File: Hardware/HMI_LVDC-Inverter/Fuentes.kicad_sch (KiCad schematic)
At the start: 33 parts, among them U2 TPS74633PQWDRBRQ1, U4 AP64100SP-13

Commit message: Termino de hacer las simulaciones de los periféricos. Completo los valores de componentes en esquemáticos
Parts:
- C28: footprint Inductor_SMD:L_1206_3216Metric -> Capacitor_SMD:C_1206_3216Metric
- R16: value 680K -> 681K
- R17: value 120K -> 121K
- R18: value 510K -> 511K
- R20: value 39863 -> 40.2K
- R21: value 4759 -> 4K75
- R22: value 500K -> 499K
- R23: value 7.005K -> 6K98
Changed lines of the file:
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@@
 			)
 		)
-		(property "Footprint" "Inductor_SMD:L_1206_3216Metric"
+		(property "Footprint" "Capacitor_SMD:C_1206_3216Metric"
 			(at 153.3652 67.31 0)
 			(effects
@@
 			)
 		)
-		(property "Value" "4759"
+		(property "Value" "4K75"
 			(at 23.114 67.818 0)
 			(effects
@@
 			)
 		)
-		(property "Value" "680K"
+		(property "Value" "681K"
 			(at 215.392 34.29 0)
 			(effects
@@
 			)
 		)
-		(property "Value" "120K"
+		(property "Value" "121K"
 			(at 217.17 44.45 0)
 			(effects
@@
 			)
 		)
-		(property "Value" "7.005K"
+		(property "Value" "6K98"
 			(at 114.554 70.612 0)
 			(effects
@@
 			)
 		)
-		(property "Value" "39863"
+		(property "Value" "40.2K"
 			(at 23.114 57.658 0)
 			(effects
@@
 			)
 		)
-		(property "Value" "510K"
+		(property "Value" "511K"
 			(at 251.206 34.29 0)
 			(effects
@@
 			)
 		)
-		(property "Value" "500K"
+		(property "Value" "499K"
 			(at 92.964 80.518 0)
 			(effects

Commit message: Terminado el esquemático del HMI
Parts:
- removed R14: 1.5M, symbol Device:R_US
- removed R15: 100K, symbol Device:R_US
- C21, C22, C23, C24, C25, C26, C27, C28, C8, L1, L2, R20, R21, R22, R23, R24, R25, U4: now not fitted
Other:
- moved on the sheet: R16, R17, R18, R19

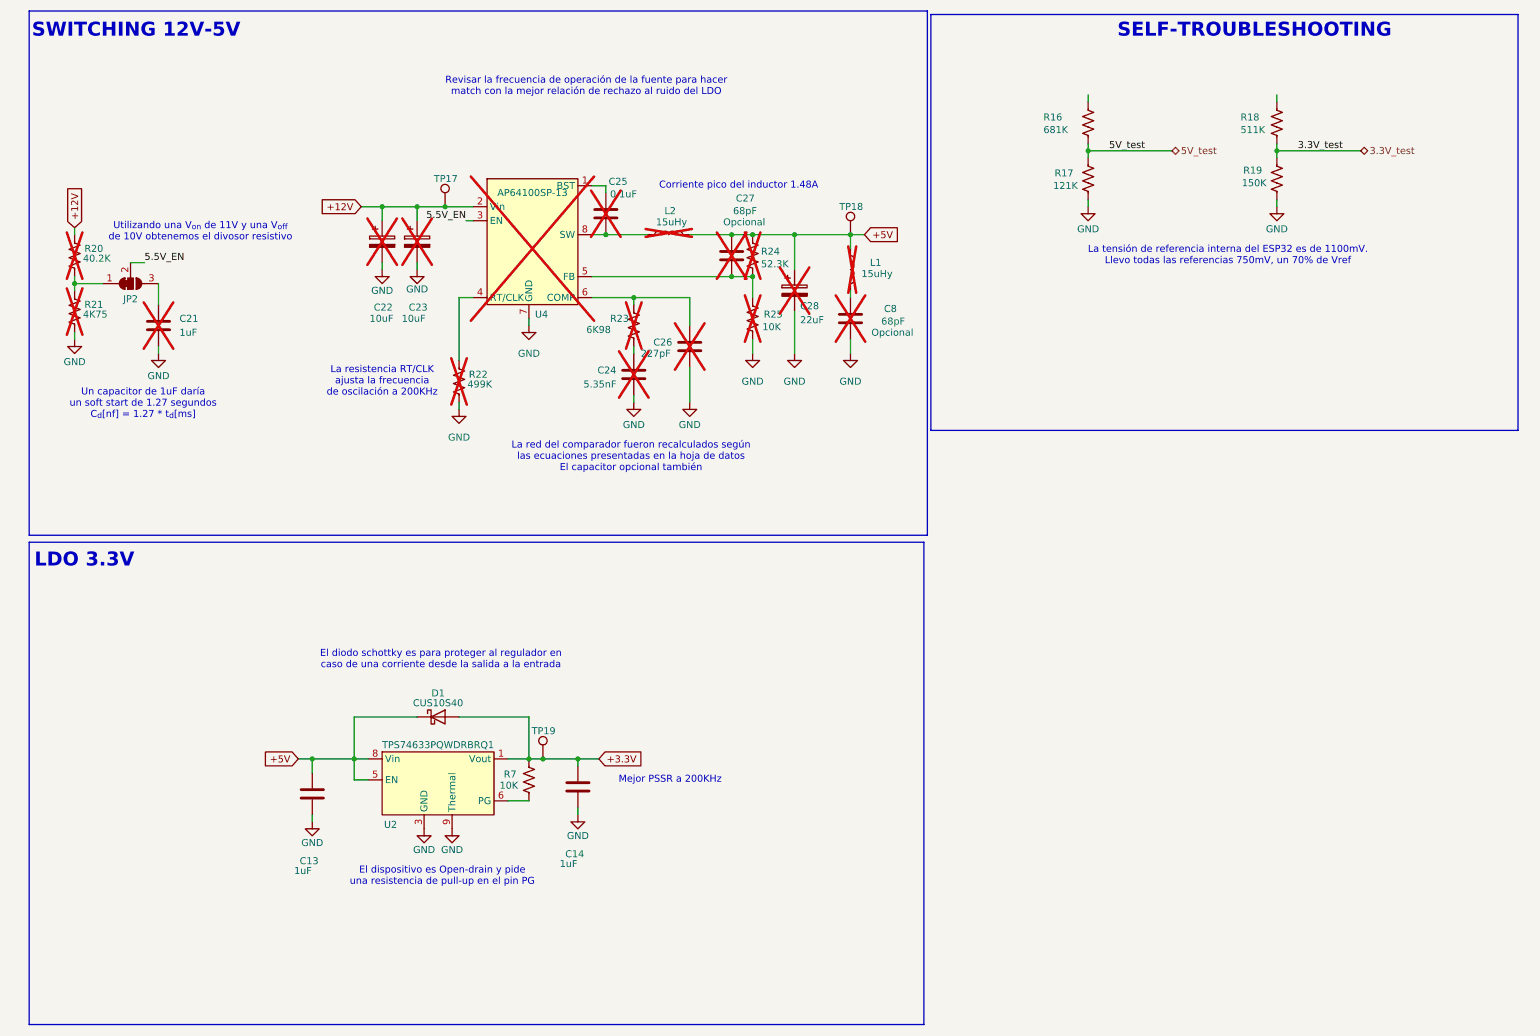
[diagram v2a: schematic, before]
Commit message: Avance con el esquemático, faltan definir algunas etiquetas que no las encontré
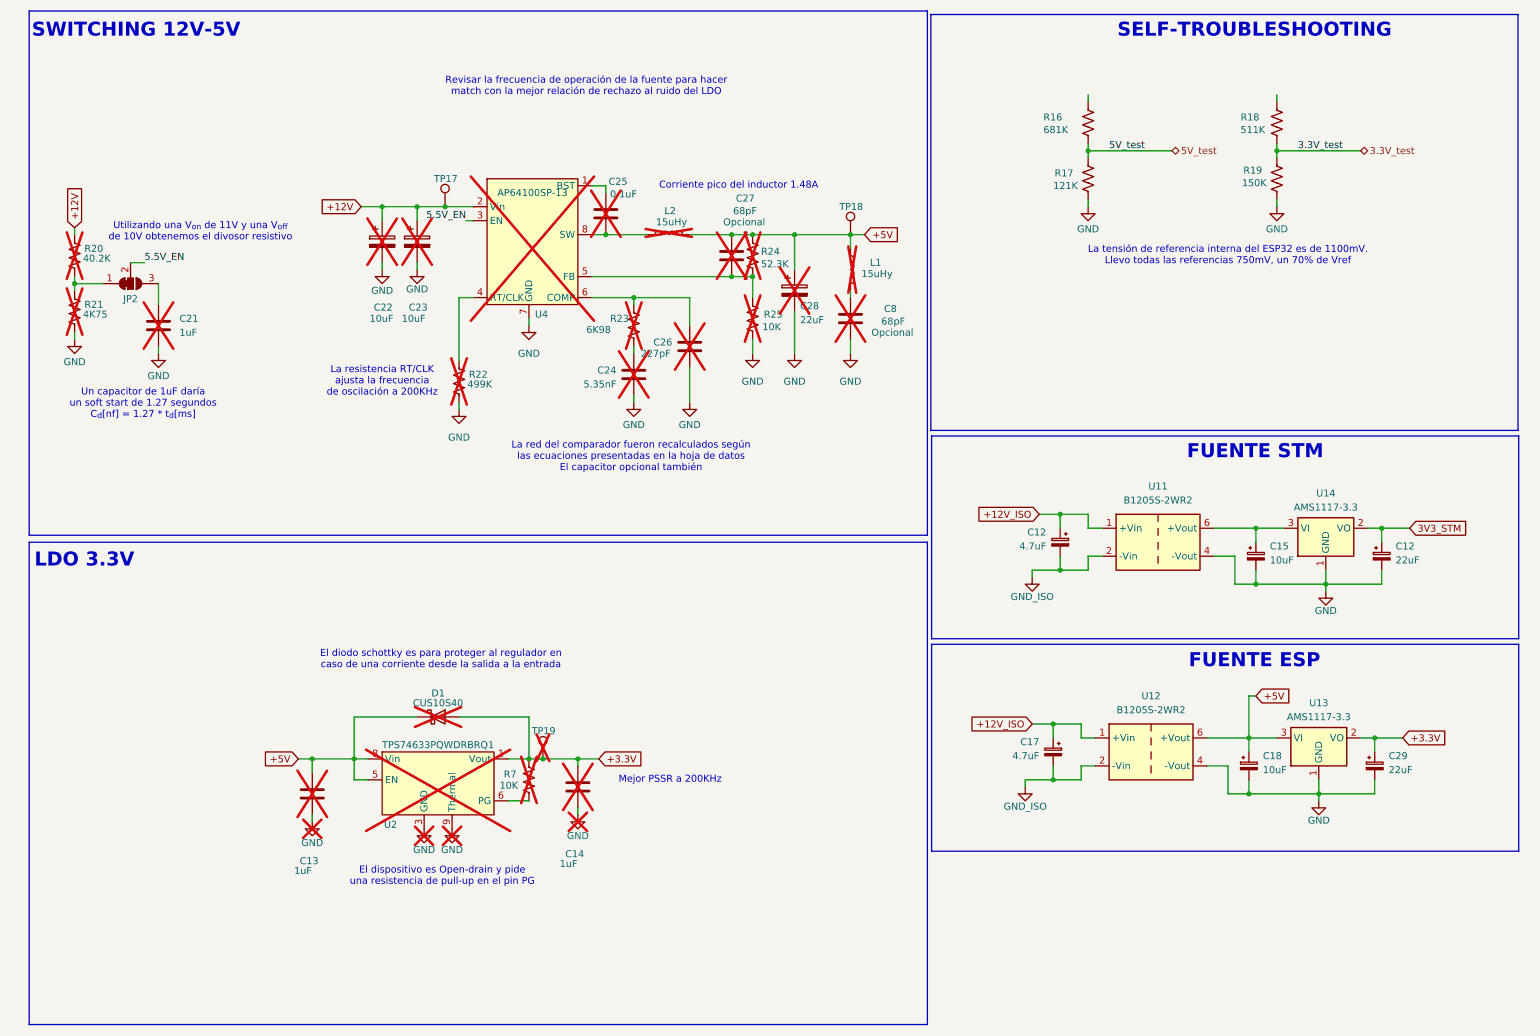
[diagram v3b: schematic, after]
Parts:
- added C12, C17: 4.7uF, Capacitor_SMD:CP_Elec_4x5.4, symbol Device:C_Polarized_Small
- added C12, C29: 22uF, Capacitor_SMD:CP_Elec_4x5.4, symbol Device:C_Polarized_Small
- added C15, C18: 10uF, Capacitor_SMD:CP_Elec_4x5.4, symbol Device:C_Polarized_Small
- added U11, U12: B1205S-2WR2, Converter_DCDC:Converter_DCDC_TRACO_TMA-05xxS_12xxS_Single_THT, symbol Converter_DCDC:TMA-1205S
- added U13, U14: AMS1117-3.3, Package_TO_SOT_SMD:SOT-223-3_TabPin2, symbol Regulator_Linear:AMS1117-3.3
- C13, C14, D1, R7, TP19, U2: now not fitted
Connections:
- net +3.3V: now also C29.1, U13.2 (VO)
- net +5V: now also C18.1, U12.6 (+Vout), U13.3 (VI)
- net GND: now also C12.2, C15.2, C18.2, C29.2, U11.4 (-Vout), U12.4 (-Vout), U13.1 (GND), U14.1 (GND)
- new net: C15.1, U11.6 (+Vout), U14.3 (VI)
- new net +12V_ISO: C12.1, C17.1, U11.1 (+Vin), U12.1 (+Vin)
- new net 3V3_STM: C12.1, U14.2 (VO)
- new net GND_ISO: C12.2, C17.2, U11.2 (-Vin), U12.2 (-Vin)
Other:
- note added: "FUENTE ESP"
- note added: "FUENTE STM"

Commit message: Terminado todo el conexionado eléctrico esquemático
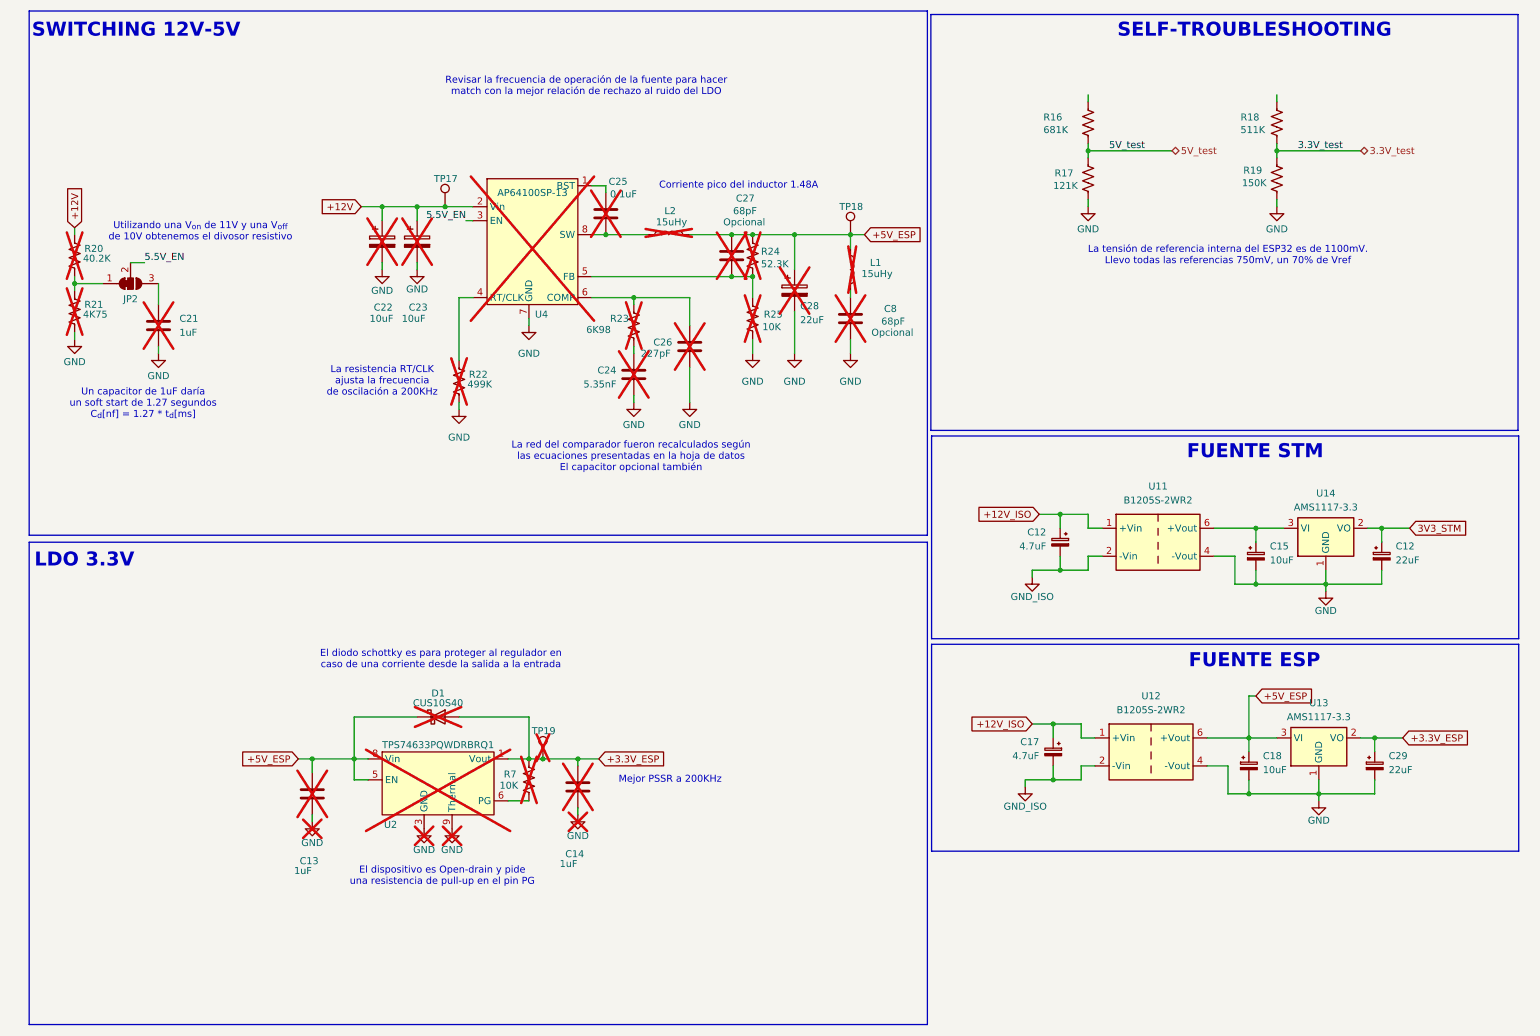
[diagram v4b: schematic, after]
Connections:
- net +3.3V renamed +3.3V_ESP
- net +5V renamed +5V_ESP
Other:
- company: (none) -> Andrenacci - Carra
- title: (none) -> Variador de frecuencia LVDC
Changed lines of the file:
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@@
 	(generator_version "9.0")
 	(paper "A4")
+	(title_block
+		(title "Variador de frecuencia LVDC")
+		(date "2025-08-05")
+		(rev "0")
+		(company "Andrenacci - Carra")
+	)
 	(rectangle
 		(start 177.165 13.335)
@@
 		)
 	)
-	(global_label "+5V"
+	(global_label "+5V_ESP"
 		(shape input)
 		(at 236.22 137.16 0)
@@
 		)
 	)
-	(global_label "+3.3V"
+	(global_label "+3.3V_ESP"
 		(shape input)
 		(at 262.89 144.78 0)
@@
 		)
 	)
-	(global_label "+5V"
+	(global_label "+5V_ESP"
 		(shape input)
 		(at 62.23 148.59 180)
@@
 		)
 	)
-	(global_label "+3.3V"
+	(global_label "+3.3V_ESP"
 		(shape input)
 		(at 116.84 148.59 0)
@@
 		)
 	)
-	(global_label "+5V"
+	(global_label "+5V_ESP"
 		(shape input)
 		(at 165.1 53.34 0)
@@
 			(justify left bottom)
 		)
-		(property "Netclass" "+5V"
+		(property "Netclass" "+5V_ESP"
 			(at 62.738 144.018 0)
 			(effects
@@
 			(justify left bottom)
 		)
-		(property "Netclass" "+3.3V"
+		(property "Netclass" "+3.3V_ESP"
 			(at 255.016 140.208 0)
 			(effects
@@
 			(justify left bottom)
 		)
-		(property "Netclass" "+3.3V"
+		(property "Netclass" "+3.3V_ESP"
 			(at 110.236 144.018 0)
 			(effects
@@
 			(justify left bottom)
 		)
-		(property "Netclass" "+5V"
+		(property "Netclass" "+5V_ESP"
 			(at 150.622 48.768 0)
 			(effects
@@
 			(justify left bottom)
 		)
-		(property "Netclass" "+3.3V"
+		(property "Netclass" "+3.3V_ESP"
 			(at 237.236 23.368 0)
 			(effects
@@
 		(length 2.54)
 		(shape round)
-		(at 231.14 144.78 0)
+		(at 229.87 144.78 0)
 		(effects
 			(font
@@
 			(justify left bottom)
 		)
-		(property "Netclass" "+5V"
-			(at 229.362 140.208 0)
+		(property "Netclass" "+5V_ESP"
+			(at 225.298 140.208 0)
 			(effects
 				(font
@@
 		)
 		(property "Component Class" ""
-			(at -64.77 77.47 0)
+			(at -66.04 77.47 0)
 			(effects
 				(font
@@
 			(justify left bottom)
 		)
-		(property "Netclass" "+5V"
+		(property "Netclass" "+5V_ESP"
 			(at 203.962 23.368 0)
 			(effects

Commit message: Agregado de los componentes con links de compra en KiCAD a excepción de los conectores
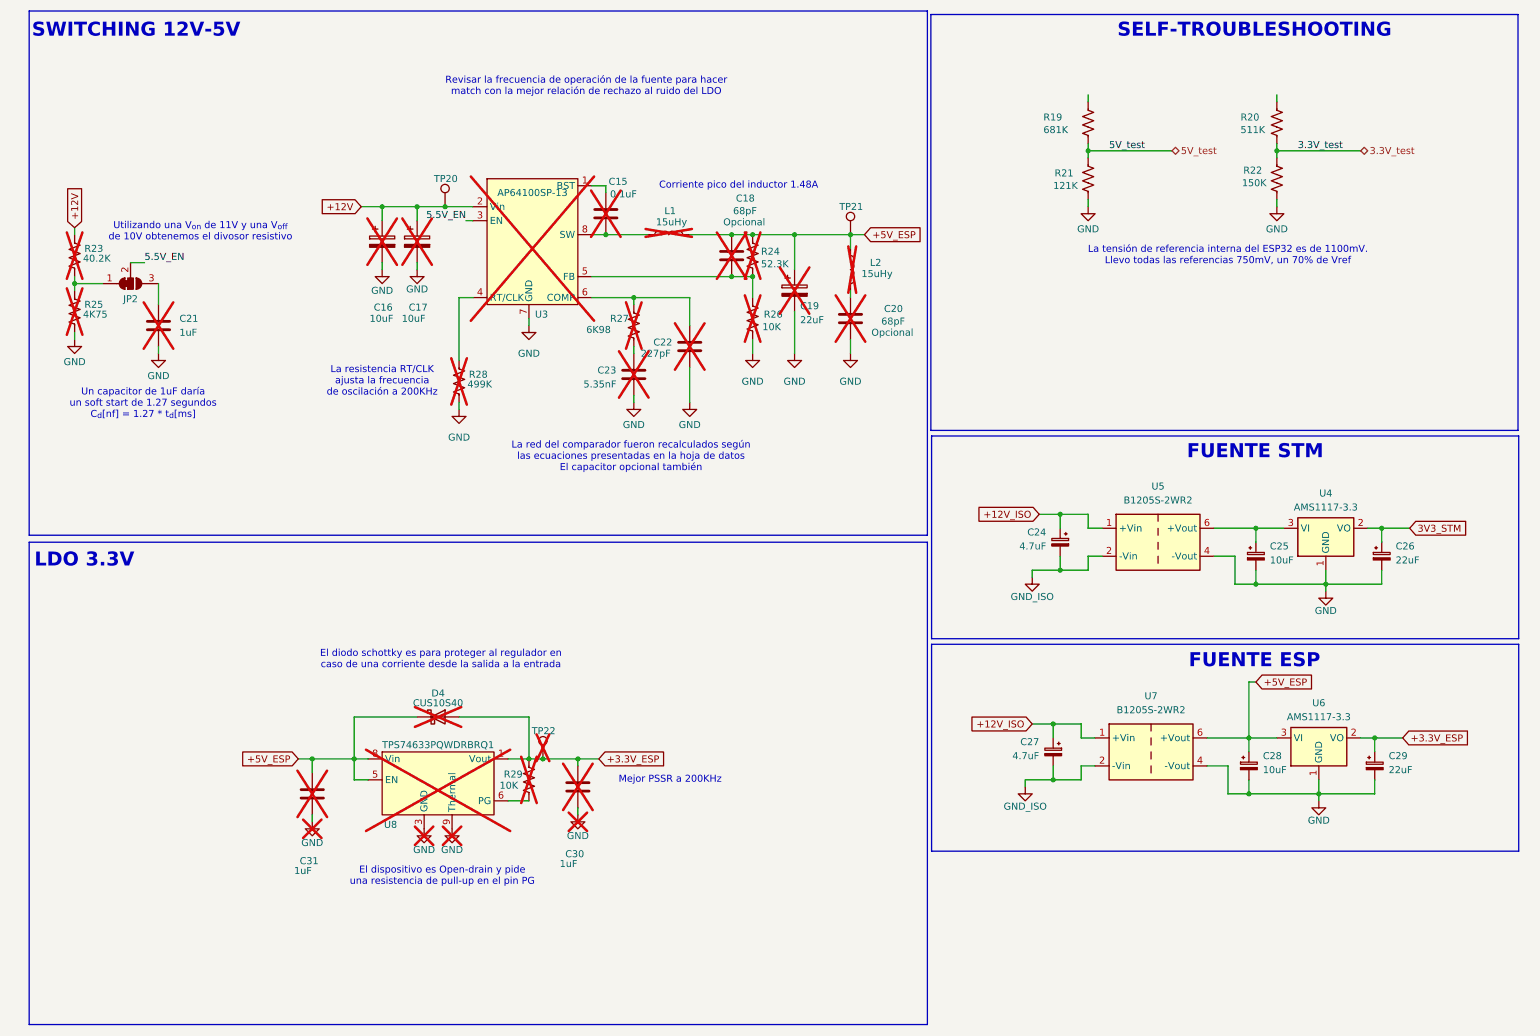
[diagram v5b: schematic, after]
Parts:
- C15: renamed from C25; Manufacturer (none) -> https://ar.mouser.com/ProductDetail/YAGEO/CC0603KRX7R7BB104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; currier https://ar.mouser.com/ProductDetail/YAGEO/CC0603KRX7R7BB104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 -> (none)
- C18: renamed from C27; Manufacturer (none) -> https://ar.mouser.com/ProductDetail/KYOCERA-AVX/06035C680KA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; currier https://ar.mouser.com/ProductDetail/KYOCERA-AVX/06035C680KA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 -> (none)
- C19: renamed from C28; Manufacturer (none) -> https://ar.mouser.com/ProductDetail/TAIYO-YUDEN/EMK316BB722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; currier https://ar.mouser.com/ProductDetail/TAIYO-YUDEN/EMK316BB722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 -> (none)
- C20: renamed from C8; Manufacturer (none) -> https://ar.mouser.com/ProductDetail/KYOCERA-AVX/06035C680KA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; currier https://ar.mouser.com/ProductDetail/KYOCERA-AVX/06035C680KA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 -> (none)
- C24: renamed from C12; footprint Capacitor_SMD:CP_Elec_4x5.4 -> Capacitor_SMD:C_0603_1608Metric; Compra (none) -> https://www.lcsc.com/product-detail/C22399629.html?s_z=n_4.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; Footprint checked (none) -> Yes; Manufacturer (none) -> HRE; Price (none) -> 0.0779; Symbol checked (none) -> Yes
- C25: renamed from C15; Compra (none) -> https://www.lcsc.com/product-detail/C72485.html; Footprint checked (none) -> Yes; Manufacturer (none) -> Roquang; Price (none) -> 0.0192; Symbol checked (none) -> Yes
- C26: renamed from C12; Compra (none) -> https://www.lcsc.com/product-detail/C72502.html; Footprint checked (none) -> Yes; Manufacturer (none) -> Roquang; Price (none) -> 0.0204; Symbol checked (none) -> Yes
- C27: renamed from C17; footprint Capacitor_SMD:CP_Elec_4x5.4 -> Capacitor_SMD:C_0603_1608Metric; Compra (none) -> https://www.lcsc.com/product-detail/C22399629.html?s_z=n_4.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; Footprint checked (none) -> Yes; Manufacturer (none) -> HRE; Price (none) -> 0.0779; Symbol checked (none) -> Yes
- C28: renamed from C18; Compra (none) -> https://www.lcsc.com/product-detail/C72485.html; Footprint checked (none) -> Yes; Manufacturer (none) -> Roquang; Price (none) -> 0.0192; Symbol checked (none) -> Yes
- C29: Compra (none) -> https://www.lcsc.com/product-detail/C72502.html; Footprint checked (none) -> Yes; Manufacturer (none) -> Roquang; Price (none) -> 0.0204; Symbol checked (none) -> Yes
- D4: renamed from D1; Manufacturer (none) -> https://ar.mouser.com/ProductDetail/757-CUS521H3F; currier https://ar.mouser.com/ProductDetail/757-CUS521H3F -> (none)
- R19: renamed from R16; footprint (none) -> Resistor_SMD:R_0603_1608Metric_Pad0.98x0.95mm_HandSolder; Compra (none) -> https://www.lcsc.com/product-detail/C403328.html; Footprint checked (none) -> Yes; Manufacturer (none) -> PANASONIC; Price (none) -> 0.0095; Symbol checked (none) -> Yes
- R20: renamed from R18; footprint (none) -> Resistor_SMD:R_0603_1608Metric_Pad0.98x0.95mm_HandSolder; Compra (none) -> https://www.lcsc.com/product-detail/C227946.html; Footprint checked (none) -> Yes; Manufacturer (none) -> YAGEO; Price (none) -> 0.0019; Symbol checked (none) -> Yes
- R21: renamed from R17; footprint (none) -> Resistor_SMD:R_0603_1608Metric_Pad0.98x0.95mm_HandSolder; Compra (none) -> https://www.lcsc.com/product-detail/C4123956.html; Footprint checked (none) -> Yes; Manufacturer (none) -> VISHAY; Price (none) -> 0.0324; Symbol checked (none) -> Yes
- R22: renamed from R19; footprint (none) -> Resistor_SMD:R_0603_1608Metric_Pad0.98x0.95mm_HandSolder; Compra (none) -> https://www.lcsc.com/product-detail/C2074190.html; Footprint checked (none) -> Yes; Manufacturer (none) -> VISHAY; Price (none) -> 0.0273; Symbol checked (none) -> Yes
- U3: renamed from U4; Manufacturer (none) -> https://ar.mouser.com/ProductDetail/621-AP64100SP-13; currier https://ar.mouser.com/ProductDetail/621-AP64100SP-13 -> (none)
- U4: renamed from U14; Compra (none) -> https://www.lcsc.com/product-detail/C347222.html; Footprint checked (none) -> Yes; Manufacturer (none) -> UMW; Price (none) -> 0.0400; Symbol checked (none) -> Yes
- U5: renamed from U11; Compra (none) -> https://www.lcsc.com/product-detail/C2992386.html; Manufacturer (none) -> YLPTEC; Symbol checked (none) -> Yes
- U6: renamed from U13; Compra (none) -> https://www.lcsc.com/product-detail/C347222.html; Footprint checked (none) -> Yes; Manufacturer (none) -> UMW; Price (none) -> 0.0400; Symbol checked (none) -> Yes
- U7: renamed from U12; Compra (none) -> https://www.lcsc.com/product-detail/C2992386.html; Manufacturer (none) -> YLPTEC; Symbol checked (none) -> Yes
- U8: renamed from U2; Manufacturer (none) -> https://ar.mouser.com/ProductDetail/595-PS74633PQWDRBRQ1; currier https://ar.mouser.com/ProductDetail/595-PS74633PQWDRBRQ1 -> (none)
- renumbered C22 to C16, C23 to C17, C26 to C22, C24 to C23, C14 to C30, C13 to C31, L2 to L1, L1 to L2, R20 to R23, R21 to R25, R25 to R26, R23 to R27, R22 to R28, R7 to R29, TP17 to TP20, TP18 to TP21, TP19 to TP22
